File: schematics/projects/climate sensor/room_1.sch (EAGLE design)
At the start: 8 parts

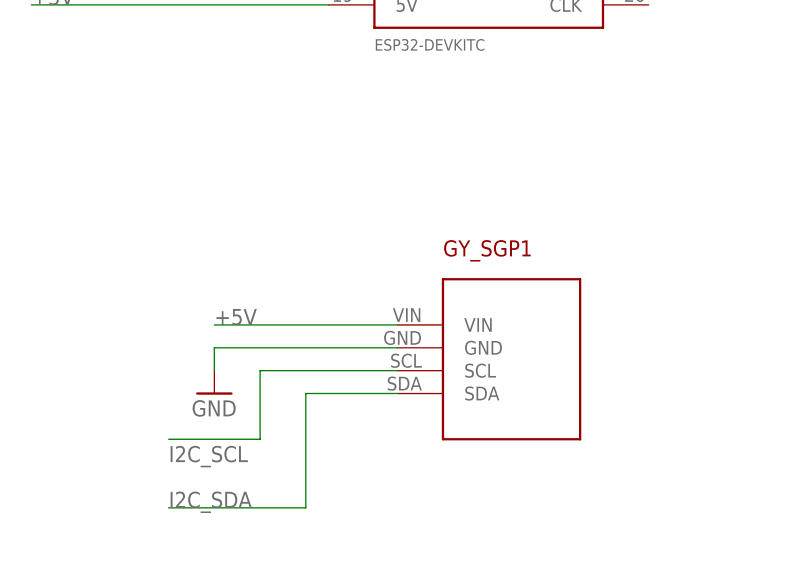
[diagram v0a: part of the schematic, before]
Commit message: added eagle board files for low-voltage schemas
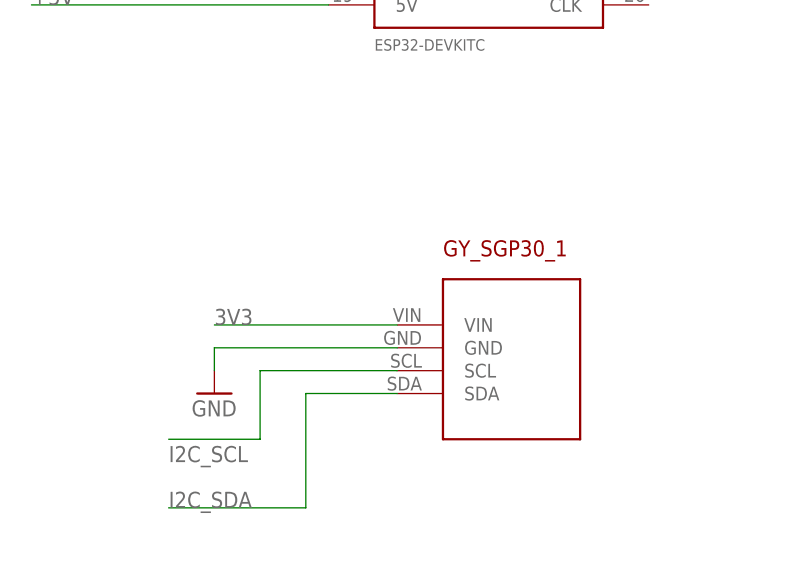
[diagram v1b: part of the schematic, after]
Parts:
- renumbered GY_SGP1 to GY_SGP30_1
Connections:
- net +5V: no longer GY_SGP30_1.VIN
- net 3V3: now also GY_SGP30_1.VIN
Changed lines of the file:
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@@
 <schematic_group name="ESP1"/>
 <schematic_group name="PMS1"/>
-<schematic_group name="GY-SGP1"/>
+<schematic_group name="GY_SGP30"/>
 <schematic_group name="MH_Z19B_CO1"/>
 <schematic_group name="BME_280_TEMP_HUM1"/>
@@
 <part name="R1" library="my_devices" deviceset="R" device="" value="600"/>
 <part name="GND6" library="supply1" library_urn="urn:adsk.eagle:library:371" deviceset="GND" device=""/>
-<part name="GY_SGP1" library="my_devices" deviceset="GY-SGP30" device=""/>
+<part name="GY_SGP30_1" library="my_devices" deviceset="GY-SGP30" device=""/>
 <part name="U$11" library="my_devices" deviceset="MH_Z19B" device=""/>
 <part name="GND13" library="supply1" library_urn="urn:adsk.eagle:library:371" deviceset="GND" device=""/>
@@
 <attribute name="VALUE" x="-8.89" y="-34.29" size="1.778" layer="94"/>
 </instance>
-<instance part="GND6" gate="1" x="76.2" y="-5.08" smashed="yes" grouprefs="GY-SGP1">
+<instance part="GND6" gate="1" x="76.2" y="-5.08" smashed="yes" grouprefs="GY_SGP30">
 <attribute name="VALUE" x="73.66" y="-7.62" size="1.778" layer="96"/>
 </instance>
-<instance part="GY_SGP1" gate="G$1" x="104.14" y="0" smashed="yes" grouprefs="GY-SGP1">
+<instance part="GY_SGP30_1" gate="G$1" x="104.14" y="0" smashed="yes" grouprefs="GY_SGP30">
 <attribute name="NAME" x="101.6" y="10.16" size="1.778" layer="94"/>
 </instance>
@@
 </segment>
 <segment>
-<wire x1="96.52" y1="0" x2="76.2" y2="0" width="0.1524" layer="91" grouprefs="GY-SGP1"/>
+<wire x1="96.52" y1="0" x2="76.2" y2="0" width="0.1524" layer="91" grouprefs="GY_SGP30"/>
 <pinref part="GND6" gate="1" pin="GND"/>
-<wire x1="76.2" y1="0" x2="76.2" y2="-2.54" width="0.1524" layer="91" grouprefs="GY-SGP1"/>
-<pinref part="GY_SGP1" gate="G$1" pin="GND"/>
+<wire x1="76.2" y1="0" x2="76.2" y2="-2.54" width="0.1524" layer="91" grouprefs="GY_SGP30"/>
+<pinref part="GY_SGP30_1" gate="G$1" pin="GND"/>
 </segment>
 <segment>
@@
 </segment>
 <segment>
-<wire x1="96.52" y1="2.54" x2="76.2" y2="2.54" width="0.1524" layer="91" grouprefs="GY-SGP1"/>
-<label x="76.2" y="2.54" size="1.778" layer="95" grouprefs="GY-SGP1"/>
-<pinref part="GY_SGP1" gate="G$1" pin="VIN"/>
-</segment>
-<segment>
 <pinref part="U$11" gate="G$1" pin="VCC"/>
 <wire x1="187.96" y1="5.08" x2="167.64" y2="5.08" width="0.1524" layer="91" grouprefs="MH_Z19B_CO1"/>
@@
 </segment>
 <segment>
-<wire x1="96.52" y1="-2.54" x2="81.28" y2="-2.54" width="0.1524" layer="91" grouprefs="GY-SGP1"/>
-<wire x1="81.28" y1="-2.54" x2="81.28" y2="-10.16" width="0.1524" layer="91" grouprefs="GY-SGP1"/>
-<wire x1="81.28" y1="-10.16" x2="71.12" y2="-10.16" width="0.1524" layer="91" grouprefs="GY-SGP1"/>
-<label x="71.12" y="-12.7" size="1.778" layer="95" grouprefs="GY-SGP1"/>
-<pinref part="GY_SGP1" gate="G$1" pin="SCL"/>
+<wire x1="96.52" y1="-2.54" x2="81.28" y2="-2.54" width="0.1524" layer="91" grouprefs="GY_SGP30"/>
+<wire x1="81.28" y1="-2.54" x2="81.28" y2="-10.16" width="0.1524" layer="91" grouprefs="GY_SGP30"/>
+<wire x1="81.28" y1="-10.16" x2="71.12" y2="-10.16" width="0.1524" layer="91" grouprefs="GY_SGP30"/>
+<label x="71.12" y="-12.7" size="1.778" layer="95" grouprefs="GY_SGP30"/>
+<pinref part="GY_SGP30_1" gate="G$1" pin="SCL"/>
 </segment>
 <segment>
@@
 </segment>
 <segment>
-<wire x1="96.52" y1="-5.08" x2="86.36" y2="-5.08" width="0.1524" layer="91" grouprefs="GY-SGP1"/>
-<wire x1="86.36" y1="-5.08" x2="86.36" y2="-17.78" width="0.1524" layer="91" grouprefs="GY-SGP1"/>
-<wire x1="86.36" y1="-17.78" x2="71.12" y2="-17.78" width="0.1524" layer="91" grouprefs="GY-SGP1"/>
-<label x="71.12" y="-17.78" size="1.778" layer="95" grouprefs="GY-SGP1"/>
-<pinref part="GY_SGP1" gate="G$1" pin="SDA"/>
+<wire x1="96.52" y1="-5.08" x2="86.36" y2="-5.08" width="0.1524" layer="91" grouprefs="GY_SGP30"/>
+<wire x1="86.36" y1="-5.08" x2="86.36" y2="-17.78" width="0.1524" layer="91" grouprefs="GY_SGP30"/>
+<wire x1="86.36" y1="-17.78" x2="71.12" y2="-17.78" width="0.1524" layer="91" grouprefs="GY_SGP30"/>
+<label x="71.12" y="-17.78" size="1.778" layer="95" grouprefs="GY_SGP30"/>
+<pinref part="GY_SGP30_1" gate="G$1" pin="SDA"/>
 </segment>
 <segment>
@@
 <label x="210.82" y="76.2" size="1.778" layer="95" grouprefs="BME_280_TEMP_HUM1"/>
 </segment>
-</net>
+<segment>
+<wire x1="96.52" y1="2.54" x2="76.2" y2="2.54" width="0.1524" layer="91" grouprefs="GY_SGP30"/>
+<label x="76.2" y="2.54" size="1.778" layer="95" grouprefs="GY_SGP30"/>
+<pinref part="GY_SGP30_1" gate="G$1" pin="VIN"/>
+</segment>
+</net>
